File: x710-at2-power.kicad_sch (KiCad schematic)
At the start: 121 parts, among them U9 EZX710AT2_S_LMR5

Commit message: [#86351] Rename project
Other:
- title: 10GbE Expansion -> OCuLink to 10GbE adapter

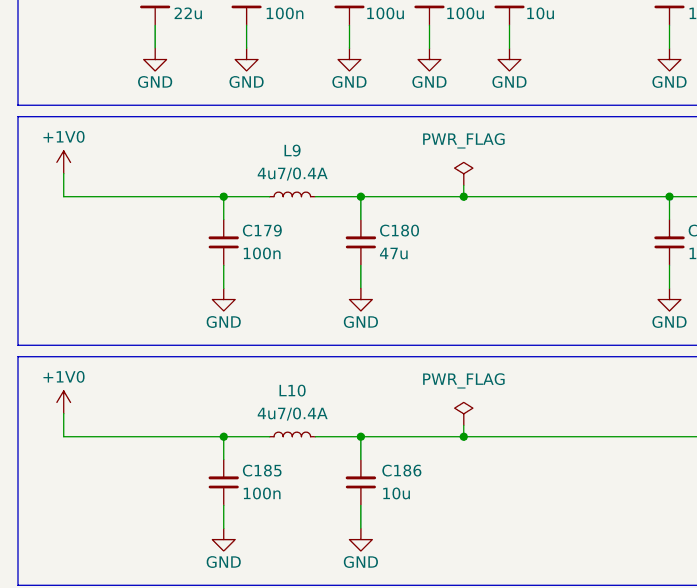
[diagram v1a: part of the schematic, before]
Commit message: [#86351] Layout power planes from X710 IC, change 4u7 inductor to one with smaller resistance
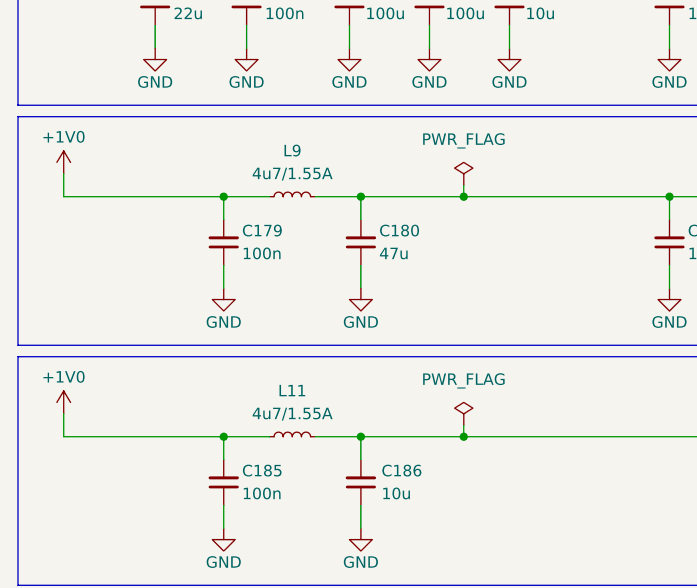
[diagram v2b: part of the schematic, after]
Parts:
- removed L10, L9: L_4u7_0.4A_0805, antmicro-footprints:L_0805_2012Metric, symbol antmicroFixedInductors:L_4u7_0.4A_0805
- added L11, L9: L_4u7_1.55A_Bourns-SRP2512A, antmicro-footprints:L_Bourns-SRP2512A, symbol antmicroFixedInductors:L_4u7_1.55A_Bourns-SRP2512A
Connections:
- net +1V0: now also L11.1, L9.1
- net XFI_PVDD: now also L11.2
- net XFI_VDD: now also L9.2

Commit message: [#86351] Minor BOM consolidation
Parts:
- C128, C130, C138, C162, C171, C179, C185, C188: value C_100n_16V_X7R_0402 -> C_100n_0402; symbol antmicroCapacitors0402:C_100n_16V_X7R_0402 -> antmicroCapacitors0402:C_100n_0402; Dielectric X7R -> X5R; MPN C0402C104J4RAC7411 -> GRM155R61H104KE14D; Manufacturer KEMET -> Murata; Voltage 16V -> 50V

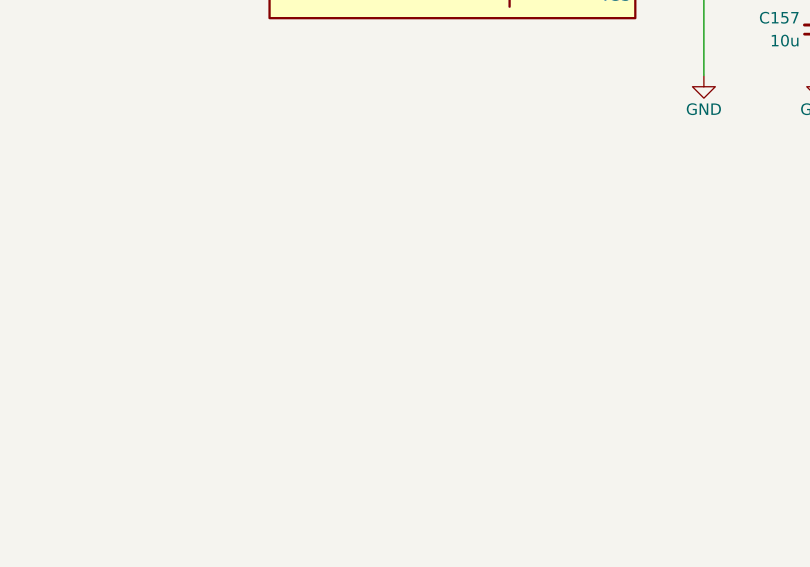
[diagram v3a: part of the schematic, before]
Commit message: [#88407] Sch: Add PCIe ref clock; Add ICT testpoints; Add fan TVS
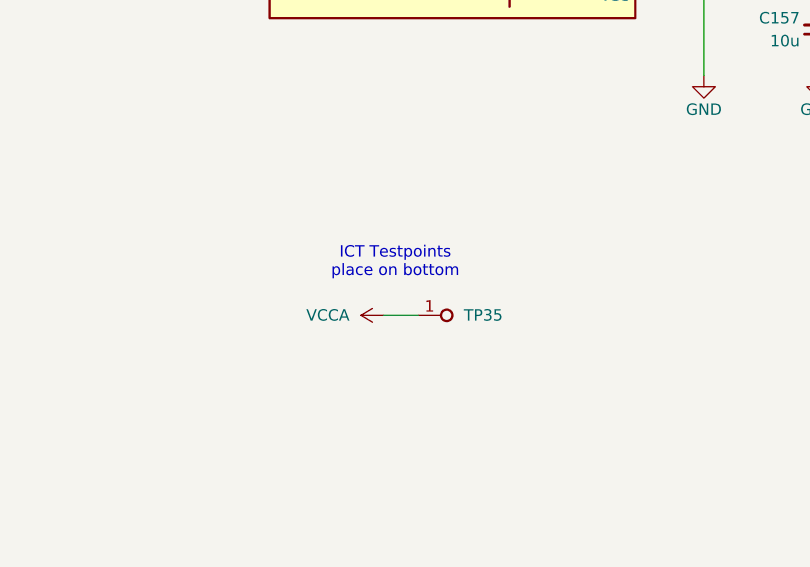
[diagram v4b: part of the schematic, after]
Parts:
- added TP35: TP_1mm_SMD, antmicro-footprints:TP_SMD_1mm, symbol antmicroTestPoints:TP_1mm_SMD
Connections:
- net VCCA: now also TP35.1
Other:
- note added: "ICT Testpoints place on bottom"
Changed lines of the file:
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@@
 	(title_block
 		(title "OCuLink to 10GbE adapter")
-		(date "2025-11-07")
+		(date "2025-12-23")
 		(rev "1.0.0")
 		(company "Antmicro Ltd")
 		(comment 1 "www.antmicro.com")
 	)
+	(text "ICT Testpoints\nplace on bottom"
+		(exclude_from_sim no)
+		(at 236.22 173.228 0)
+		(effects
+			(font
+				(size 1.27 1.27)
+			)
+		)
+	)
 	(text "X710-AT2 Power"
 		(exclude_from_sim no)
@@
 	(wire
 		(pts
+			(xy 234.95 179.07) (xy 238.76 179.07)
+		)
+		(stroke
+			(width 0)
+			(type default)
+		)
+	)
+	(wire
+		(pts
 			(xy 62.23 146.05) (xy 62.23 148.59)
 		)
@@
 	)
 	(symbol
+		(lib_id "antmicroTestPoints:TP_1mm_SMD")
+		(at 238.76 179.07 0)
+		(unit 1)
+		(exclude_from_sim no)
+		(in_bom no)
+		(on_board yes)
+		(dnp no)
+		(fields_autoplaced yes)
+		(property "Reference" "TP35"
+			(at 243.84 179.07 0)
+			(effects
+				(font
+					(size 1.27 1.27)
+					(thickness 0.15)
+				)
+				(justify left)
+			)
+		)
+		(property "Value" "TP_1mm_SMD"
+			(at 254 186.69 0)
+			(effects
+				(font
+					(size 1.27 1.27)
+					(thickness 0.15)
+				)
+				(justify left bottom)
+				(hide yes)
+			)
+		)
+		(property "Footprint" "antmicro-footprints:TP_SMD_1mm"
+			(at 254 189.23 0)
+			(effects
+				(font
+					(size 1.27 1.27)
+					(thickness 0.15)
+				)
+				(justify left bottom)
+				(hide yes)
+			)
+		)
+		(property "Datasheet" ""
+			(at 256.54 191.77 0)
+			(effects
+				(font
+					(size 1.27 1.27)
+					(thickness 0.15)
+				)
+				(justify left bottom)
+				(hide yes)
+			)
+		)
+		(property "Description" "Test point 1mm SMD"
+			(at 254 199.39 0)
+			(effects
+				(font
+					(size 1.27 1.27)
+				)
+				(justify left bottom)
+				(hide yes)
+			)
+		)
+		(property "MPN" ""
+			(at 238.76 179.07 0)
+			(effects
+				(font
+					(size 1.27 1.27)
+				)
+				(hide yes)
+			)
+		)
+		(property "Manufacturer" ""
+			(at 238.76 179.07 0)
+			(effects
+				(font
+					(size 1.27 1.27)
+				)
+				(hide yes)
+			)
+		)
+		(property "Author" "Antmicro"
+			(at 254 194.31 0)
+			(effects
+				(font
+					(size 1.27 1.27)
+					(thickness 0.15)
+				)
+				(justify left bottom)
+				(hide yes)
+			)
+		)
+		(property "License" "Apache-2.0"
+			(at 254 196.85 0)
+			(effects
+				(font
+					(size 1.27 1.27)
+					(thickness 0.15)
+				)
+				(justify left bottom)
+				(hide yes)
+			)
+		)
+		(pin "1"
+		)
+		(instances
+			(project "oculink-to-10gbe-adapter"
+				(path "/04bda987-e5eb-48b4-9e90-d8211dc11b39/745fdd8b-25af-4553-a7ea-a0fa564ee0a7"
+					(reference "TP35")
+					(unit 1)
+				)
+			)
+		)
+	)
+	(symbol
 		(lib_id "antmicroCapacitors0603:C_22u_16V_0603")
 		(at 44.45 52.07 90)
@@
 					(unit 1)
 				)
+			)
+		)
+	)
+	(symbol
+		(lib_id "antmicropower:VCC")
+		(at 234.95 179.07 90)
+		(unit 1)
+		(exclude_from_sim no)
+		(in_bom yes)
+		(on_board yes)
+		(dnp no)
+		(fields_autoplaced yes)
+		(property "Reference" "#PWR0310"
+			(at 238.76 179.07 0)
+			(effects
+				(font
+					(size 1.27 1.27)
+				)
+				(hide yes)
+			)
+		)
+		(property "Value" "VCCA"
+			(at 231.14 179.0699 90)
+			(effects
+				(font
+					(size 1.27 1.27)
+				)
+				(justify left)
+			)
+		)
+		(property "Footprint" ""
+			(at 234.95 179.07 0)
+			(effects
+				(font
+					(size 1.27 1.27)
+				)
+				(hide yes)
+			)
+		)
+		(property "Datasheet" ""
+			(at 234.95 179.07 0)
+			(effects
+				(font
+					(size 1.27 1.27)
+				)
+				(hide yes)
+			)
+		)
+		(property "Description" ""
+			(at 234.95 179.07 0)
+			(effects
+				(font
+					(size 1.27 1.27)
+				)
+				(hide yes)
+			)
+		)
+		(pin "1"
+		)
+		(instances
+			(project "oculink-to-10gbe-adapter"
+				(path "/04bda987-e5eb-48b4-9e90-d8211dc11b39/745fdd8b-25af-4553-a7ea-a0fa564ee0a7"
+					(reference "#PWR0310")
+					(unit 1)
+				)
